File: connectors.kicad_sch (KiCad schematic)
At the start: 4 parts, among them J1 1861975, J2 1861975, J3 1861946, J4 SM04B-SRSS-TB

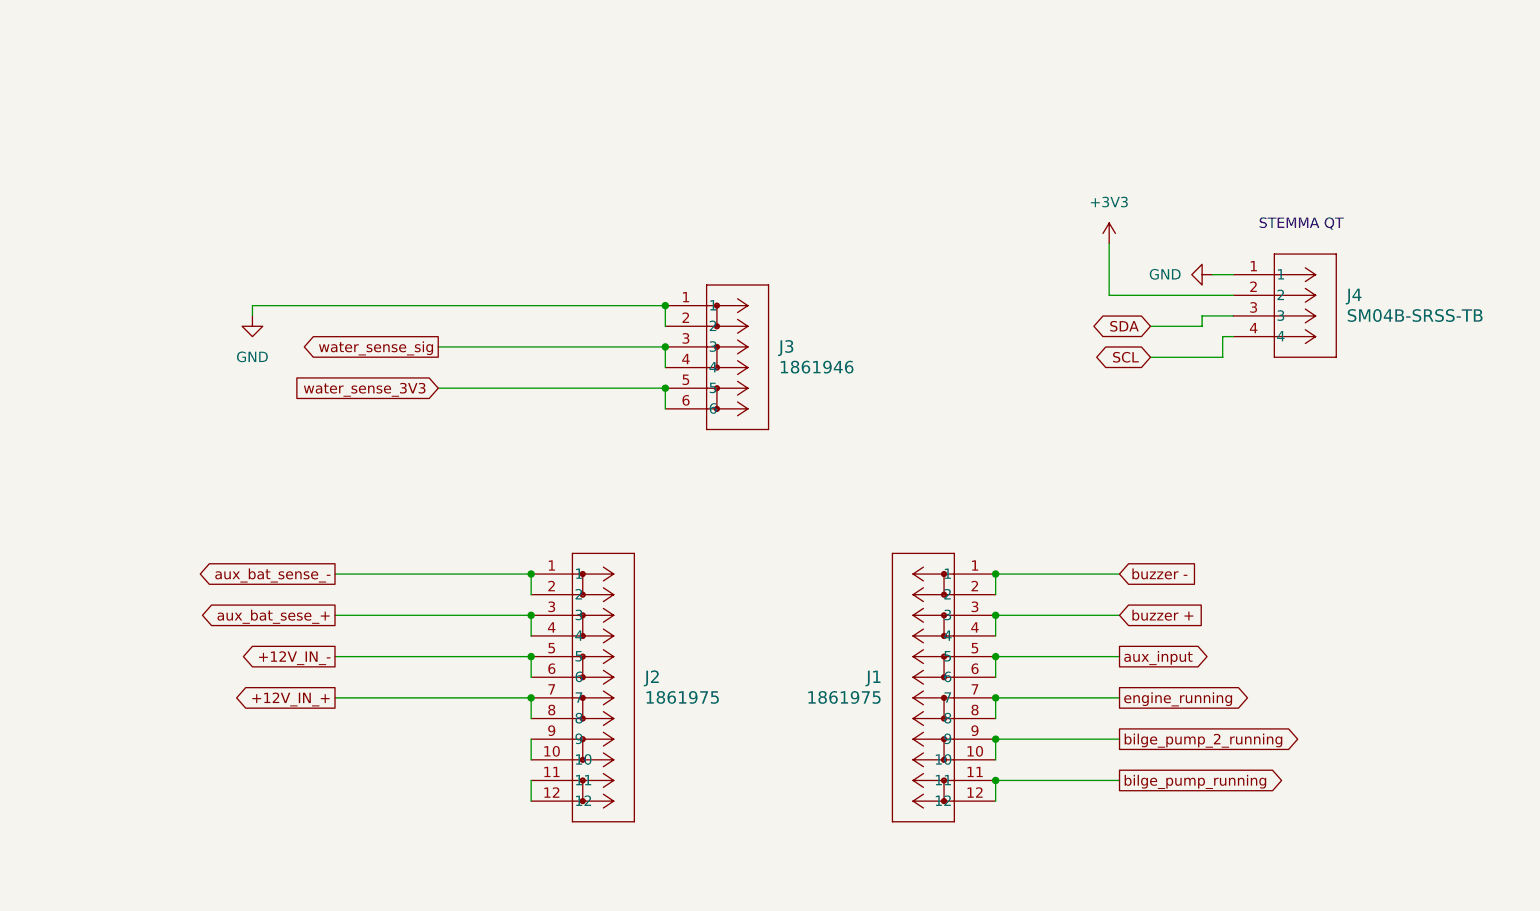
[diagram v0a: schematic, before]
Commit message: add status led, etc.
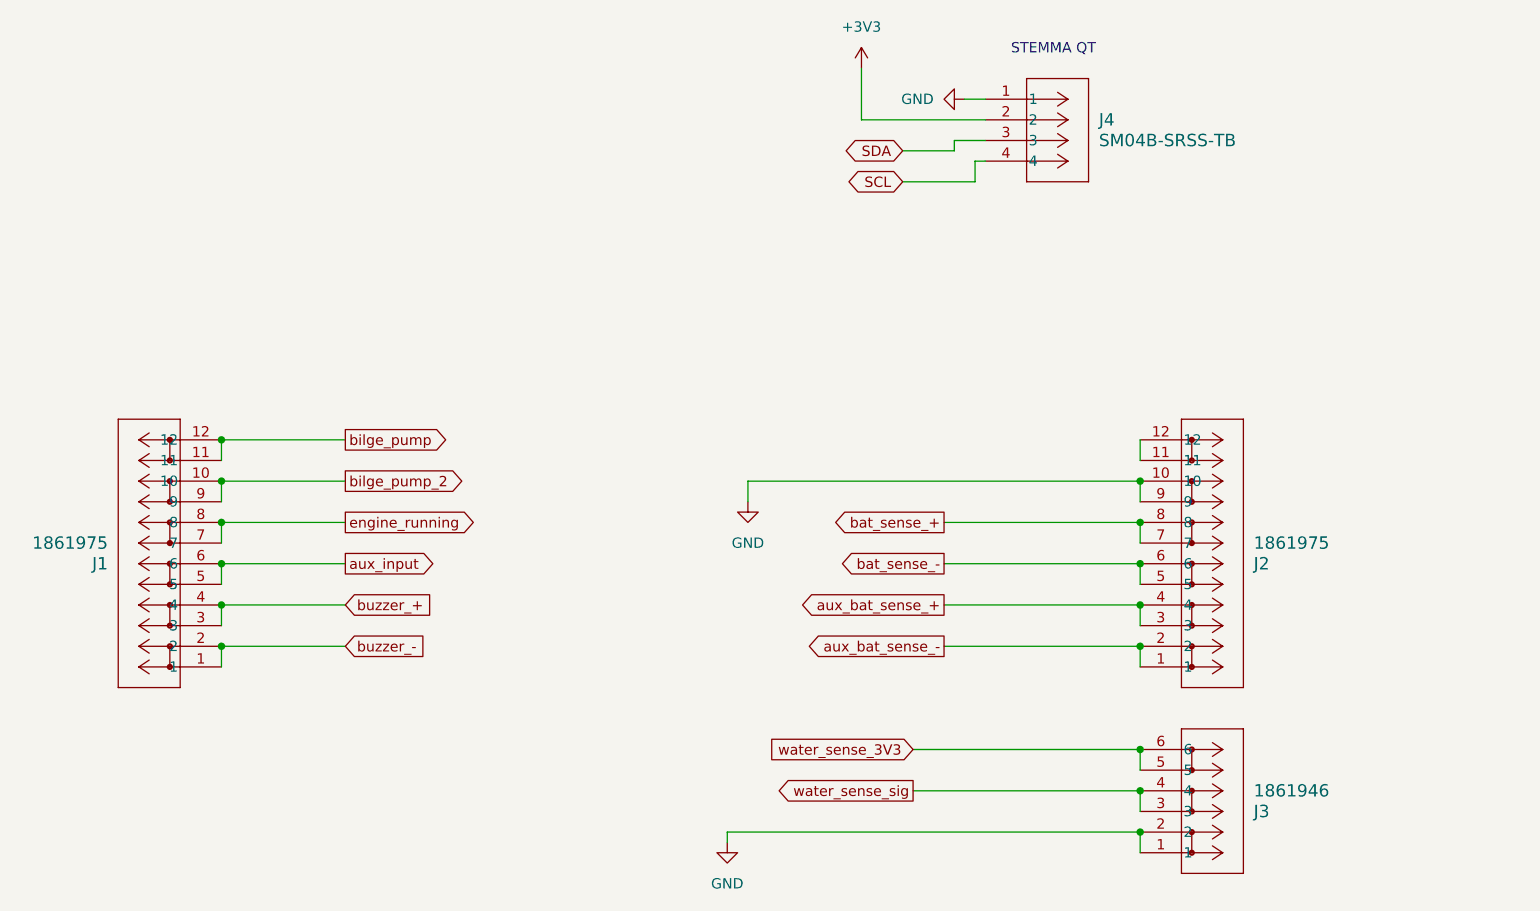
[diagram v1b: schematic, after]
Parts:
- J3: footprint 1891946:CONN_1861946 -> CONN_1861946
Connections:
- net GND: now also J2.10, J2.9
- net +12V_IN_+ renamed bat_sense_+
- net +12V_IN_- renamed bat_sense_-
- net aux_bat_sese_+ renamed aux_bat_sense_+
- net bilge_pump_2_running renamed bilge_pump_2
- net bilge_pump_running renamed bilge_pump
- net buzzer + renamed buzzer_+
- net buzzer - renamed buzzer_-
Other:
- moved on the sheet: J1, J2, J3, J4
